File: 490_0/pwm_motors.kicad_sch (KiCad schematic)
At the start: 39 parts, among them J11 S2B-XH-A, J12 S2B-XH-A, J13 S2B-XH-A, J14 S2B-XH-A, J21 S2B-XH-A, Q3 NMOS, Q4 NMOS, Q5 NMOS, Q6 NMOS, Q7 NMOS, U8 PCA9685

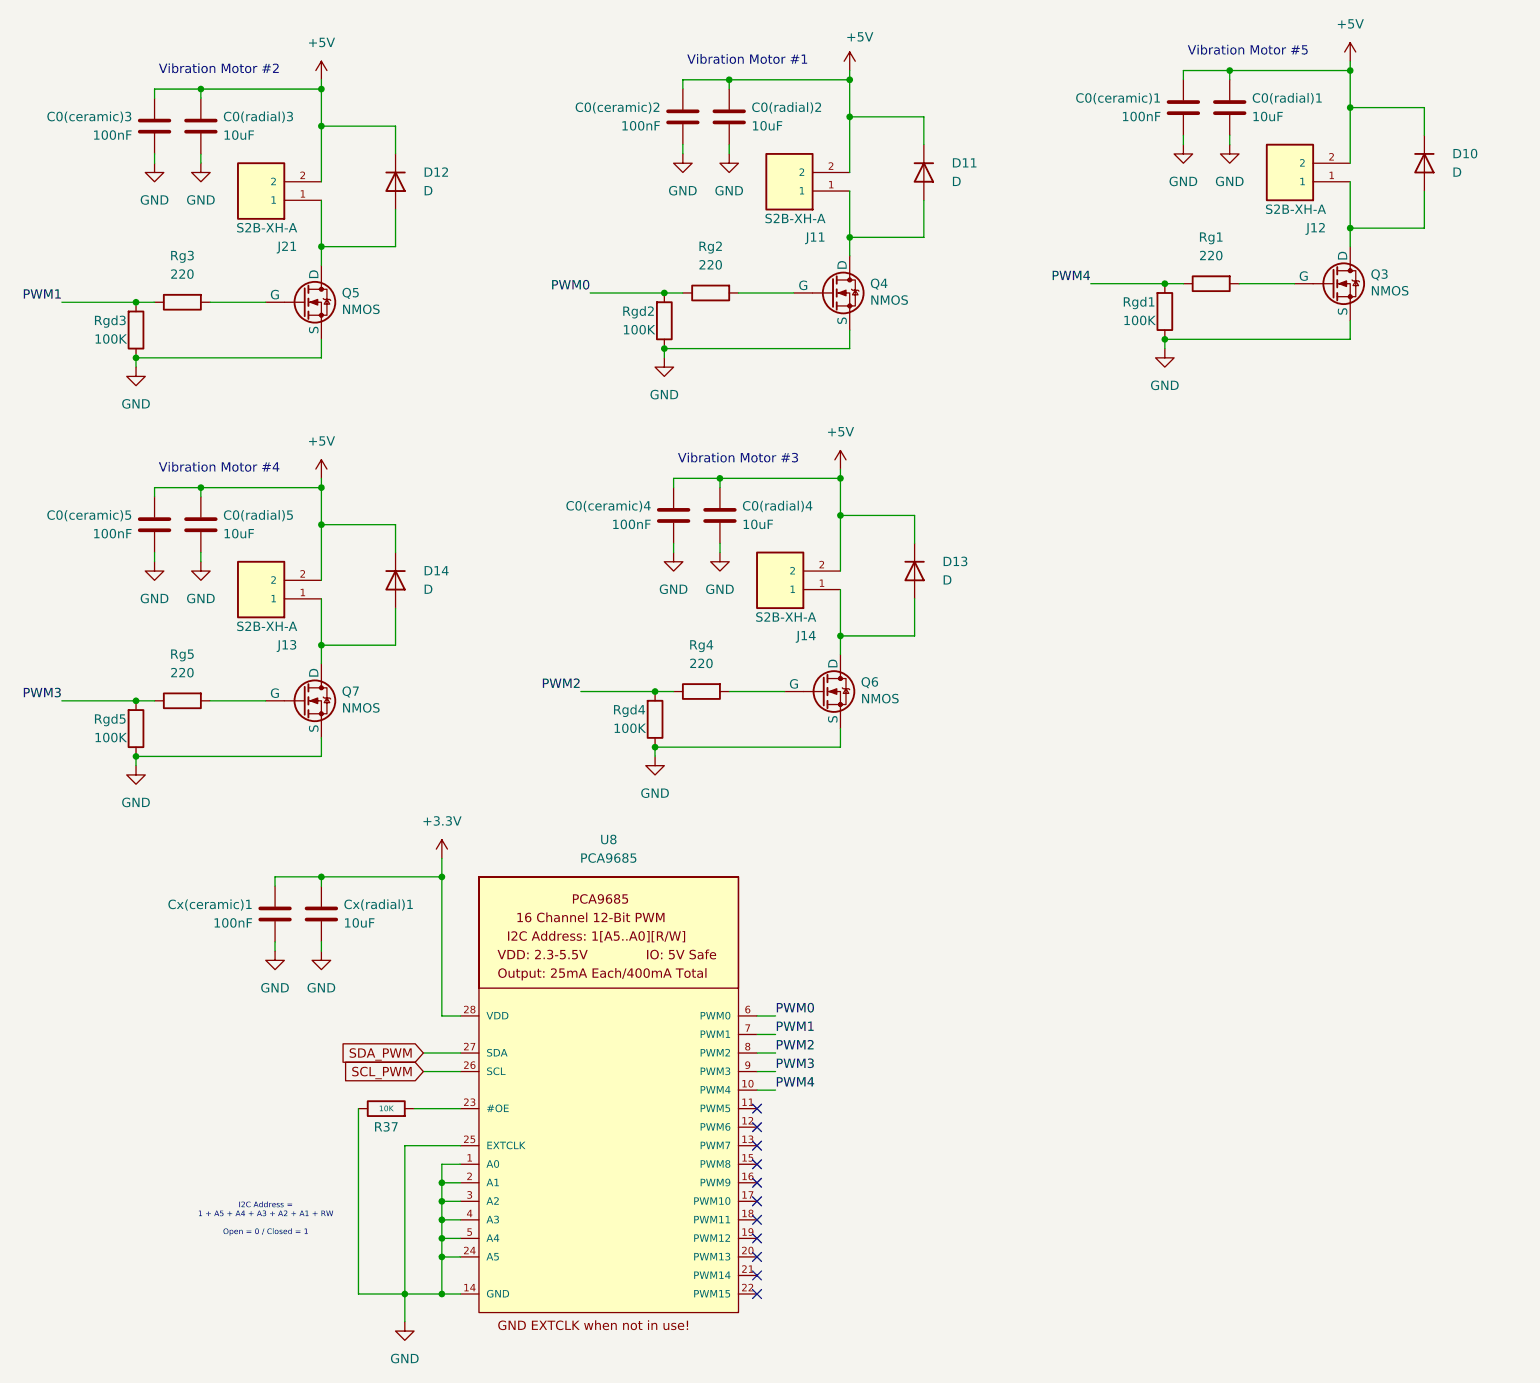
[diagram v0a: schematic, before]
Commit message: Schematic layout update
- applied hierarchical labels
- cleaned up the schematic
- finalized CM4 connections
- checked cm4 connections
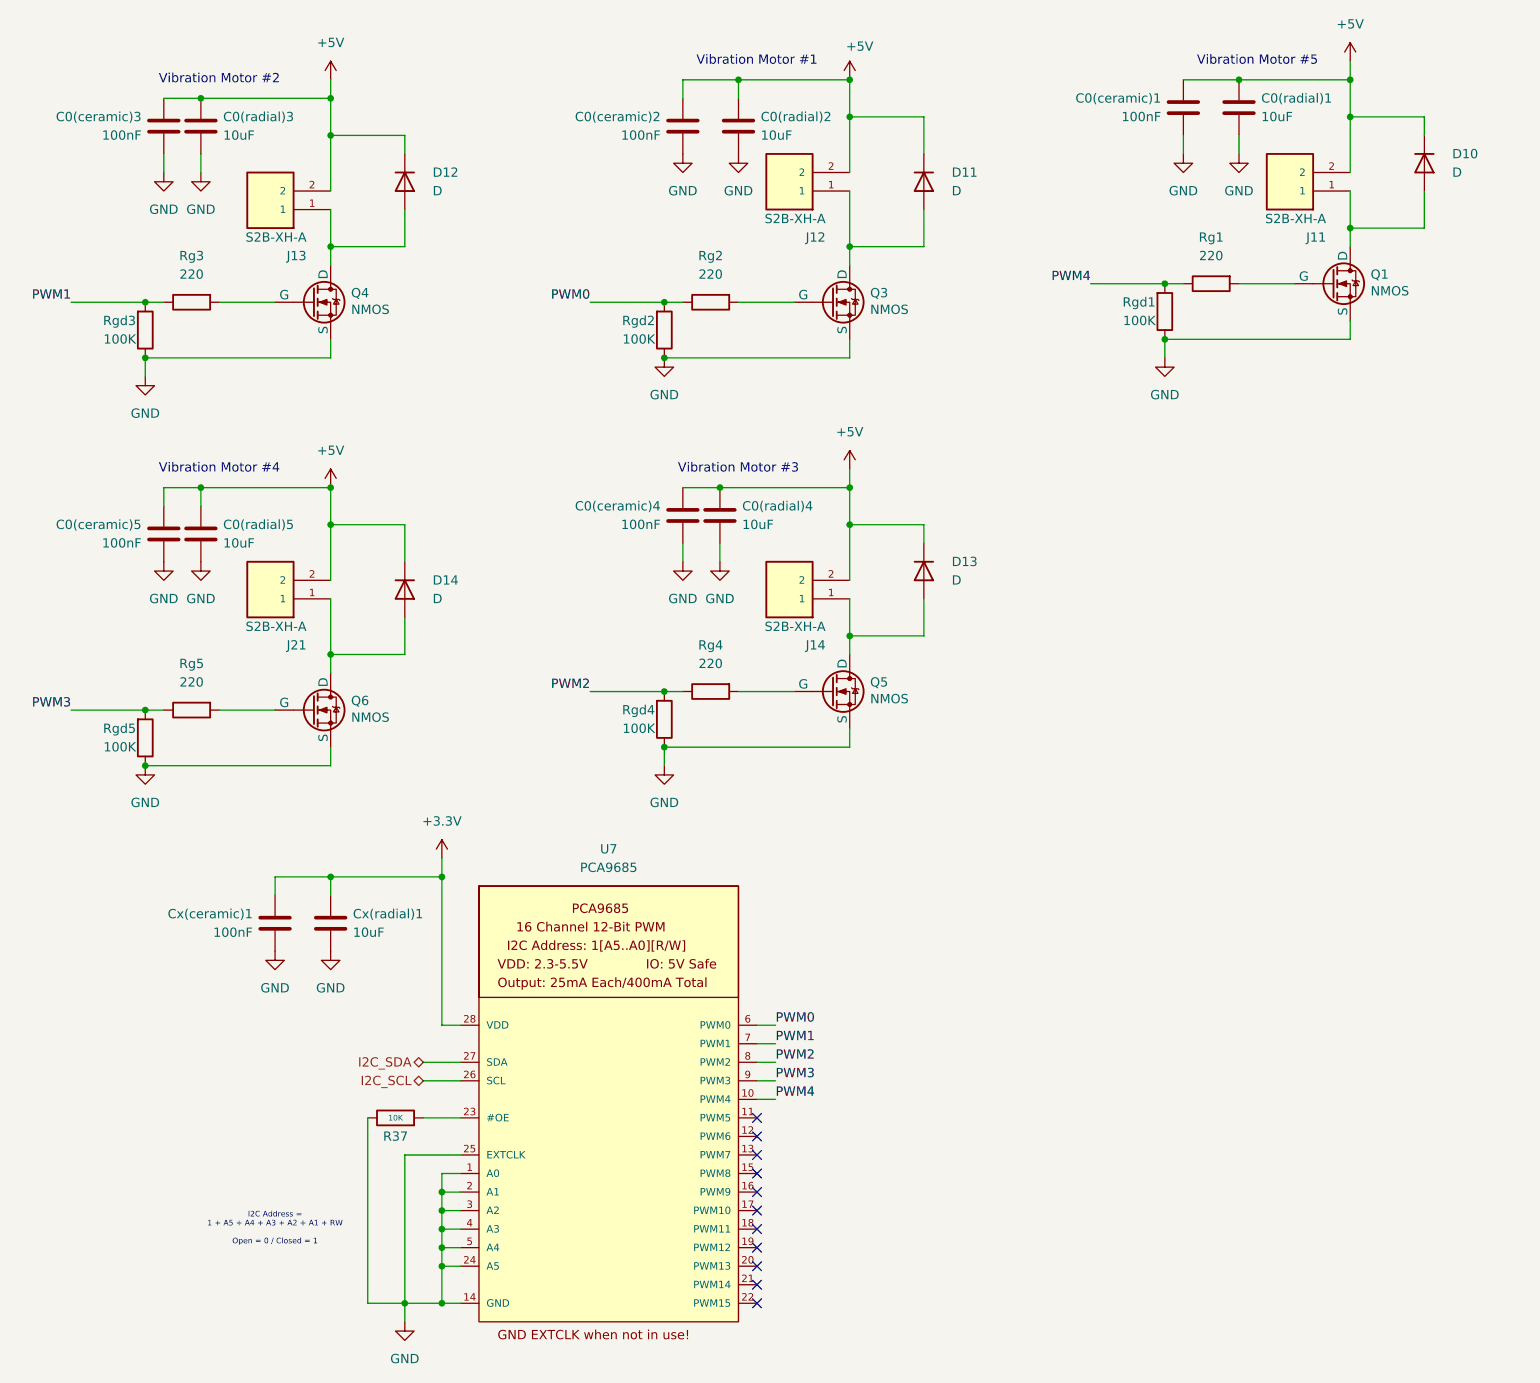
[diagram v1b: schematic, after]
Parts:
- renumbered J12 to J11, J11 to J12, J21 to J13, J13 to J21, Q3 to Q1, Q4 to Q3, Q5 to Q4, Q6 to Q5, Q7 to Q6, U8 to U7
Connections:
- net SCL_PWM renamed I2C_SCL
- net SDA_PWM renamed I2C_SDA
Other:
- moved on the sheet: C0(ceramic)2, C0(ceramic)3, C0(ceramic)4, C0(ceramic)5, C0(radial)1, C0(radial)2, C0(radial)5, Cx(ceramic)1, Cx(radial)1, D11, D12, D13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

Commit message: Power + BOM update
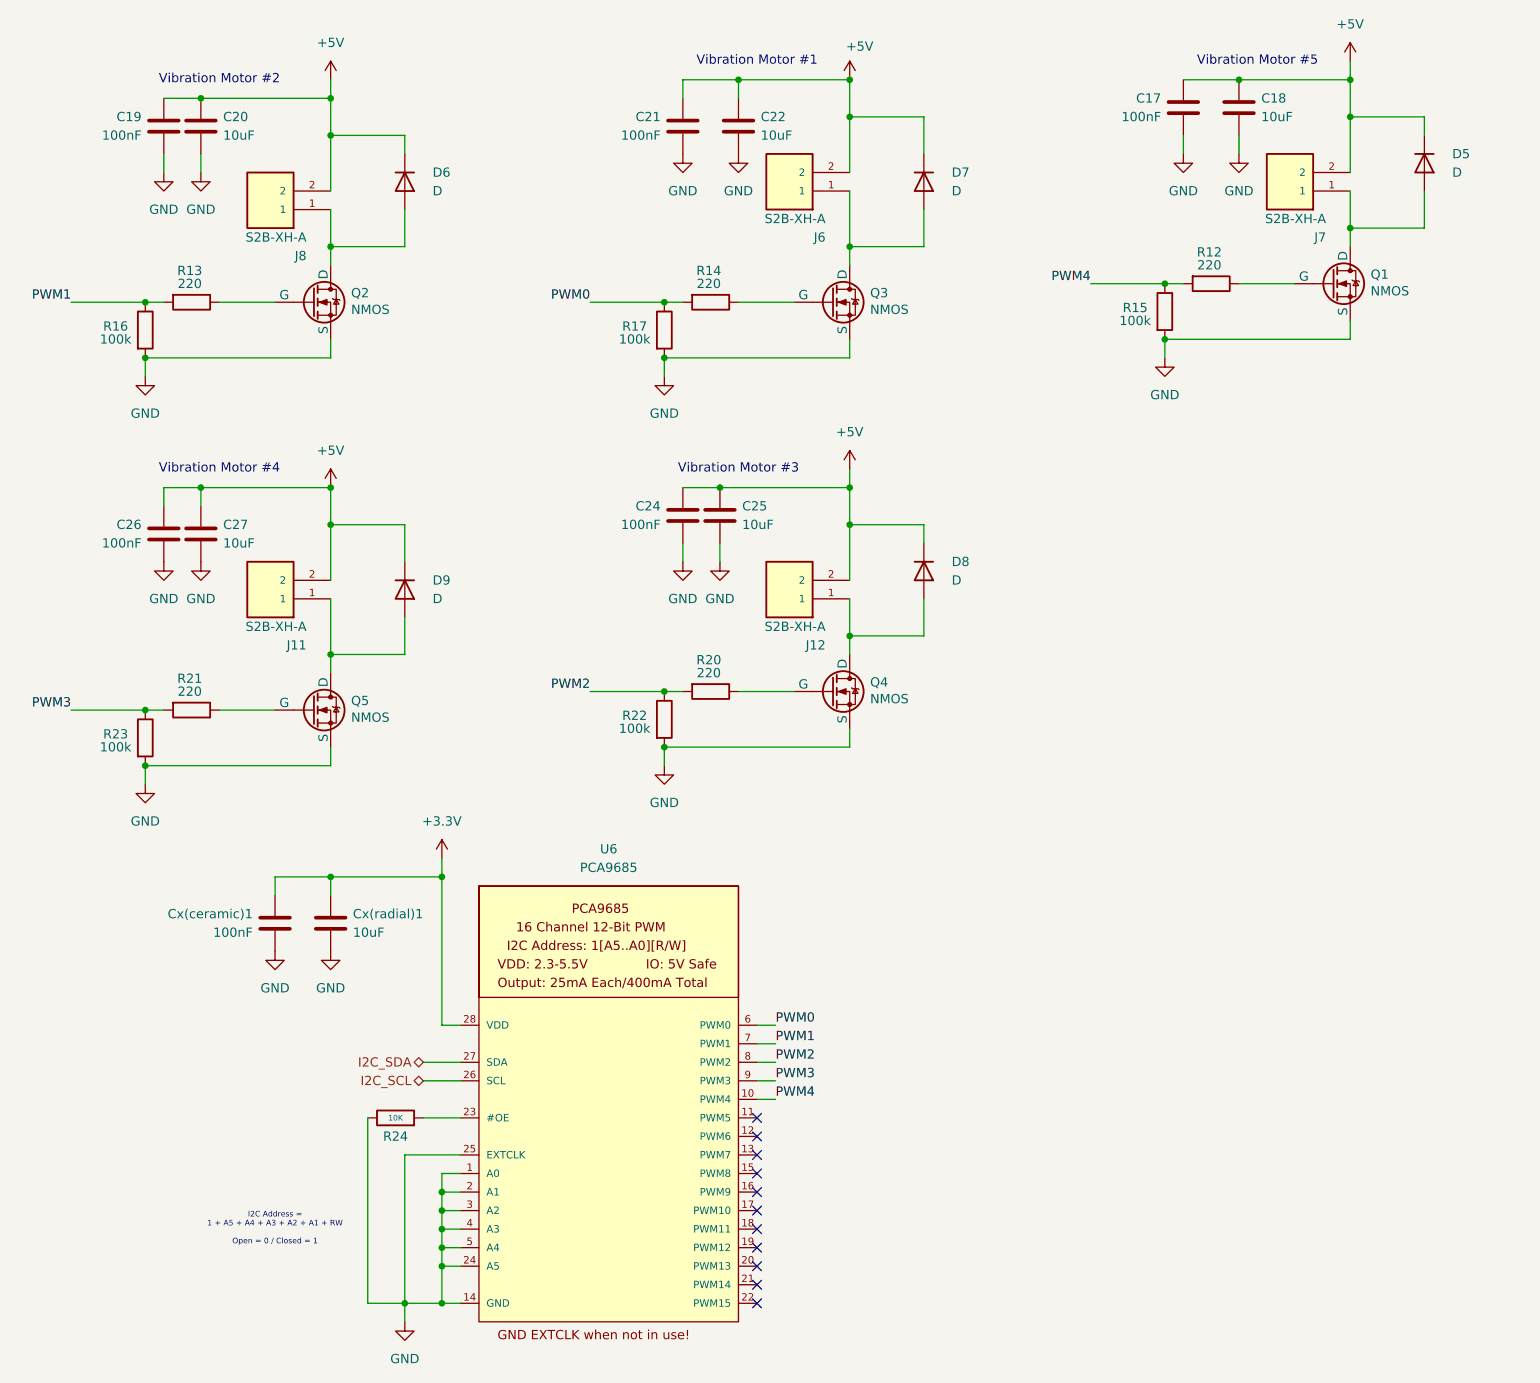
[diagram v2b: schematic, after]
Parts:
- removed Rg1, Rg2, Rg3, Rg4, Rg5: 220, symbol Device:R
- removed Rgd1, Rgd2, Rgd3, Rgd4, Rgd5: 100K, symbol Device:R
- added R12, R13, R14, R20, R21: 220, symbol Device:R
- added R15, R16, R17, R22, R23: 100k, symbol Device:R
- C17: renamed from C0(ceramic)1; footprint Capacitor_SMD:C_0603_1608Metric -> (none)
- C18: renamed from C0(radial)1; footprint Capacitor_THT:CP_Radial_D5.0mm_P2.50mm -> (none)
- C19: renamed from C0(ceramic)3; footprint Capacitor_SMD:C_0603_1608Metric -> (none)
- C20: renamed from C0(radial)3; footprint Capacitor_THT:CP_Radial_D5.0mm_P2.50mm -> (none)
- C21: renamed from C0(ceramic)2; footprint Capacitor_SMD:C_0603_1608Metric -> (none)
- C22: renamed from C0(radial)2; footprint Capacitor_THT:CP_Radial_D5.0mm_P2.50mm -> (none)
- C24: renamed from C0(ceramic)4; footprint Capacitor_SMD:C_0603_1608Metric -> (none)
- C25: renamed from C0(radial)4; footprint Capacitor_THT:CP_Radial_D5.0mm_P2.50mm -> (none)
- C26: renamed from C0(ceramic)5; footprint Capacitor_SMD:C_0603_1608Metric -> (none)
- J11: renamed from J21; footprint S2B-XH-A:JST_S2B-XH-A -> 4ms_Connector:Pins_1x08_2.54mm_TH
- J12: renamed from J14; footprint S2B-XH-A:JST_S2B-XH-A -> 4ms_Connector:Pins_1x08_2.54mm_TH
- renumbered C0(radial)5 to C27, D10 to D5, D12 to D6, D11 to D7, D13 to D8, D14 to D9, J12 to J6, J11 to J7, J13 to J8, Q4 to Q2, Q5 to Q4, Q6 to Q5, R37 to R24, U7 to U6
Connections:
- net GND: now also R15.2, R16.2, R17.2, R22.2, R23.2
- net PWM0: now also R14.2, R17.1
- net PWM1: now also R13.2, R16.1
- net PWM2: now also R20.2, R22.1
- net PWM3: now also R21.2, R23.1
- net PWM4: now also R12.2, R15.1
- net at Q4.2 (G): now also R20.1
- net at Q1.2 (G): now also R12.1
- net at Q3.2 (G): now also R14.1
- net at Q2.2 (G): now also R13.1
- net at Q5.2 (G): now also R21.1

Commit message: finished BOM
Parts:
- removed Cx(ceramic)1: 100nF, Capacitor_SMD:C_0603_1608Metric, symbol Device:C
- removed Cx(radial)1: 10uF, Capacitor_THT:CP_Radial_D5.0mm_P2.50mm, symbol Device:C
- added C48: 100n, symbol Device:C
- added C51: 10u, symbol Device:C
- C17, C19, C21, C24, C26: value 100nF -> 100n; Digikey Link (none) -> https://www.digikey.ca/en/products/detail/samsung-electro-m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; Manufacturer (none) -> Samsung Electro-Mechanics; Manufacturer Part (none) -> CL31B104KBCNNNC; Package (none) -> 1206 (3216 Metric); Price (none) -> 0.11; Supplier (none) -> DigiKey; Supplier P/N (none) -> 1276-1017-1-ND; Type (none) -> SMD, MLCC; Unit (none) -> pcs
- C18, C20, C22, C25: value 10uF -> 10u; Digikey Link (none) -> https://www.digikey.ca/en/products/detail/kemet/c1206c106k4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; Manufacturer (none) -> KEMET; Manufacturer Part (none) -> C1206C106K4RACTU; Package (none) -> 1206 (3216 Metric); Price (none) -> 0.31; Supplier (none) -> DigiKey; Supplier P/N (none) -> 399-C1206C106K4RACTUCT-ND; Type (none) -> SMD, MLCC; Unit (none) -> pcs
- C27: value 10uF -> 10u; footprint Capacitor_THT:CP_Radial_D5.0mm_P2.50mm -> (none); Digikey Link (none) -> https://www.digikey.ca/en/products/detail/kemet/c1206c106k4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; Manufacturer (none) -> KEMET; Manufacturer Part (none) -> C1206C106K4RACTU; Package (none) -> 1206 (3216 Metric); Price (none) -> 0.31; Supplier (none) -> DigiKey; Supplier P/N (none) -> 399-C1206C106K4RACTUCT-ND; Type (none) -> SMD, MLCC; Unit (none) -> pcs
- D5, D6, D7, D8, D9: value D -> 1N4148W; Digikey Link (none) -> https://www.digikey.ca/en/products/detail/diotec-semiconduc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; Manufacturer (none) -> Diotec Semiconductor; Manufacturer Part (none) -> 1N4148W; Package (none) -> SOD-123F; Price (none) -> 0.1; Supplier (none) -> DigiKey; Supplier P/N (none) -> 4878-1N4148WCT-ND; Type (none) -> SMD; Unit (none) -> pcs
- Q1, Q2, Q3, Q4, Q5: Digikey Link (none) -> https://www.digikey.ca/en/products/detail/alpha-omega-semic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; Manufacturer (none) -> Alpha & Omega Semiconductor Inc.; Manufacturer Part (none) -> AO3400A; Package (none) -> SOT-23-3; Price (none) -> 0.46; Supplier (none) -> DigiKey; Supplier P/N (none) -> 785-1000-1-ND; Type (none) -> SMD; Unit (none) -> pcs
- R24: value 10K -> 10k; Digikey Link (none) -> https://www.digikey.ca/en/products/detail/yageo/RC1206FR-07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; Manufacturer (none) -> YAGEO; Manufacturer Part (none) -> RC1206FR-0710KL; Package (none) -> 1206; Price (none) -> 0.1; Supplier (none) -> DigiKey; Supplier P/N (none) -> 311-10.0KFRCT-ND; Type (none) -> SMD; Unit (none) -> pcs
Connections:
- net +3.3V: now also C48.1, C51.1
- net GND: now also C48.2, C51.2

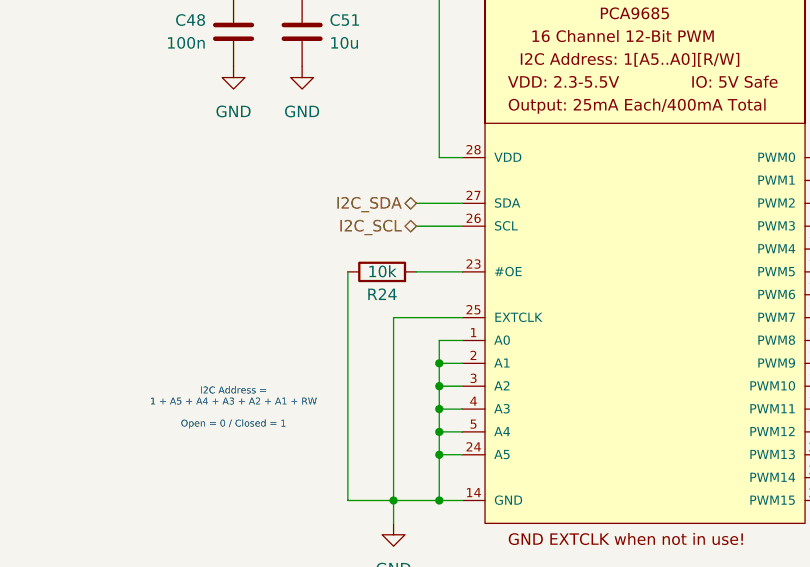
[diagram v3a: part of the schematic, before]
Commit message: Changed buck converter chip
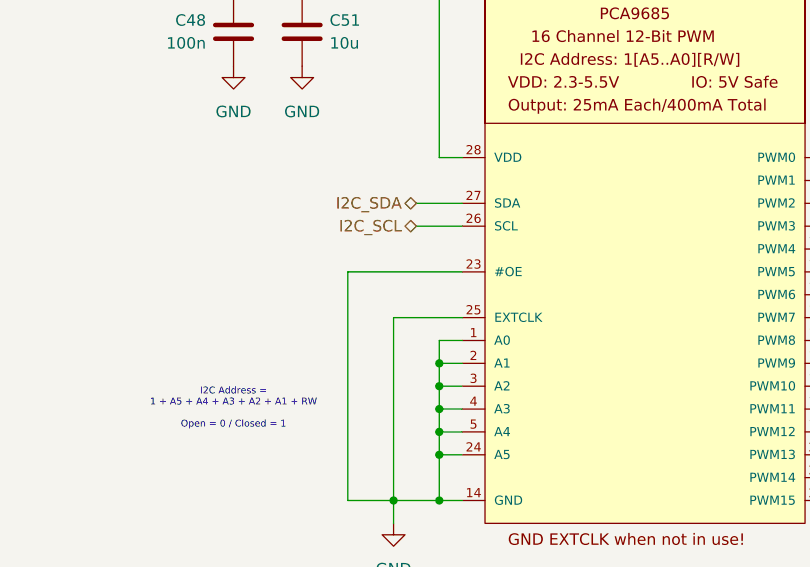
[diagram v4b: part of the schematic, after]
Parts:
- removed R24: 10k, symbol Device:R
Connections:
- net GND: now also U6.23 (#OE)
